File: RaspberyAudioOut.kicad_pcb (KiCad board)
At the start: 2 copper layers, 29 parts, among them J1 Conn_01x04, U1 LM386, U2 LM386

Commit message: Adding PDF of PCB
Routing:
- net GND: track 158.0 -> 26.6 mm

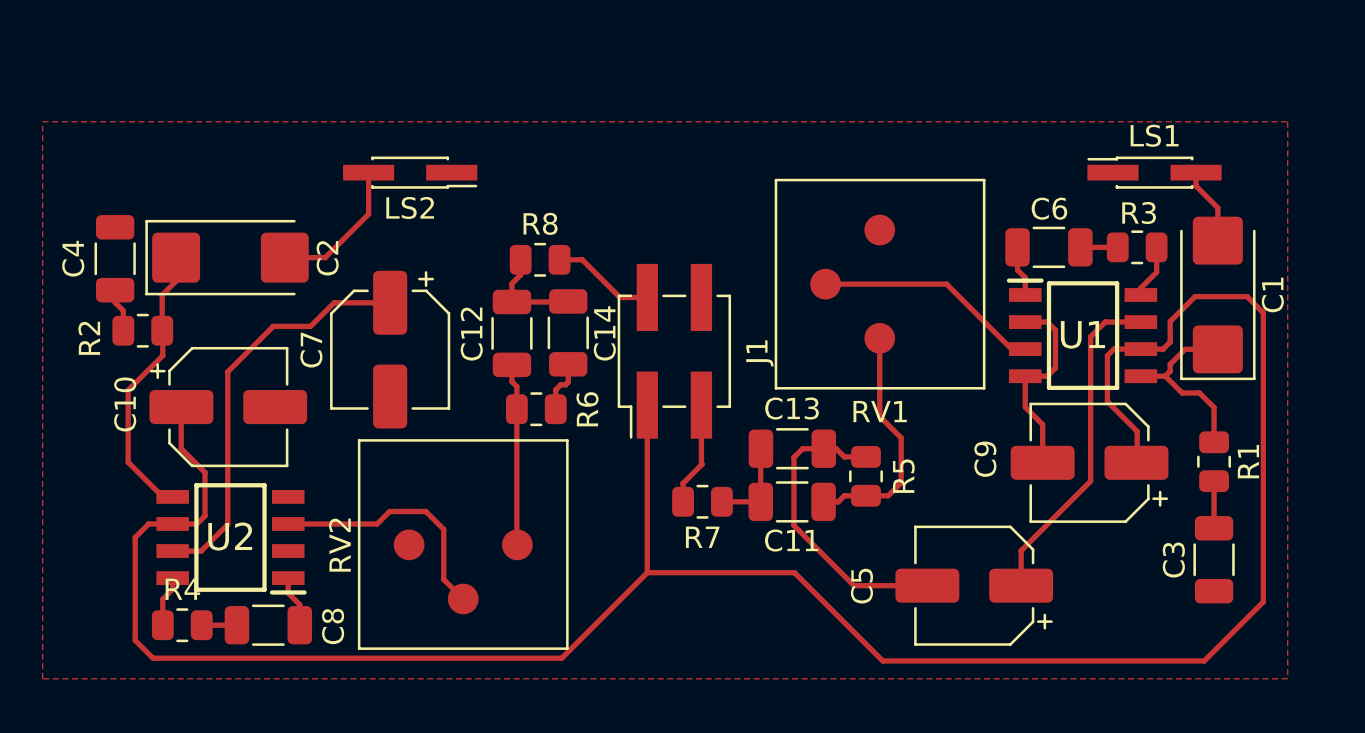
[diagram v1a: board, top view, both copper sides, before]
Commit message: Second step. Changed traces width and some components were added
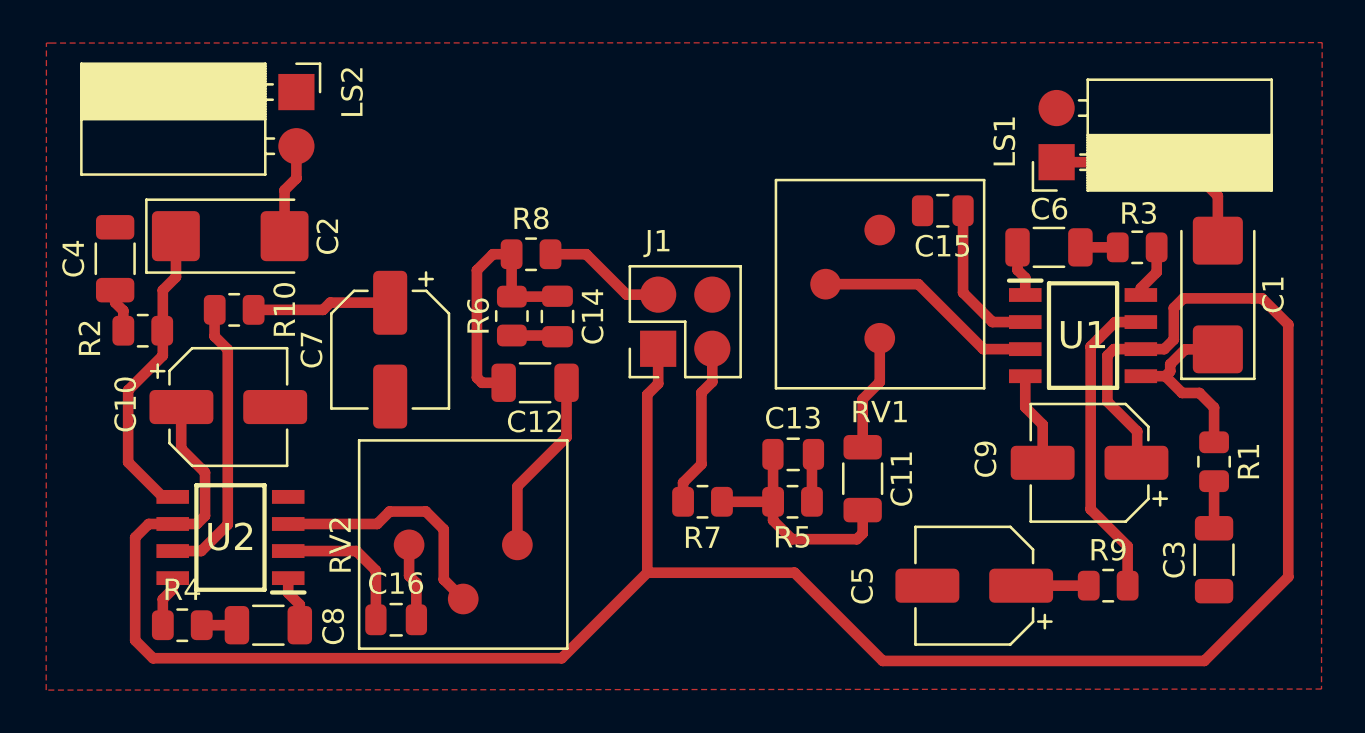
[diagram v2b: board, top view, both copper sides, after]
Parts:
- added C15: 1n, Capacitor_SMD:C_0805_2012Metric, F.Cu at (122.4, 81.2)
- added C16: 1n, Capacitor_SMD:C_0805_2012Metric, F.Cu at (96.8, 100.4)
- added R10: 10k, Resistor_SMD:R_0805_2012Metric, F.Cu at (89.2, 85.9)
- added R9: 10k, Resistor_SMD:R_0805_2012Metric, F.Cu at (130.2, 98.8)
- C13, C14: footprint Capacitor_SMD:C_1206_3216Metric -> Capacitor_SMD:C_0805_2012Metric
- J1: footprint Connector_PinHeader_2.54mm:PinHeader_2x02_P2.54mm_Vertical_SMD -> Connector_PinHeader_2.54mm:PinHeader_2x02_P2.54mm_Vertical
- LS1, LS2: footprint Connector_PinHeader_1.27mm:PinHeader_2x01_P1.27mm_Vertical_SMD -> Connector_PinSocket_2.54mm:PinSocket_1x02_P2.54mm_Horizontal
- moved LS2 6.54 mm to (92.1, 75.7), turned to 0 degrees
- moved LS1 4.62 mm to (127.7, 79.0), turned to 180 degrees
- moved R6 4.52 mm to (102.2, 86.2), turned to -90 degrees
- moved R5 3.65 mm to (115.3, 94.9), turned to 0 degrees
- moved C11 3.48 mm to (118.6, 93.8), turned to -90 degrees
- moved C12 2.56 mm to (103.3, 89.3), turned to 180 degrees
- moved C2 1.01 mm to (89.0, 82.4)
- moved C14 0.92 mm to (104.3, 86.2)
- moved J1 0.77 mm to (109.0, 87.7)
- moved R8 0.50 mm to (103.1, 83.3)
- moved C13 0.27 mm to (115.4, 92.7)
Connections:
- C11 pad 1: Net-(C11-Pad1) -> Net-(RV1-Pad3)
- C12 pad 1: Net-(C12-Pad1) -> Net-(RV2-Pad3)
- C12 pad 2: Net-(C12-Pad2) -> Net-(R6-Pad1)
- C14 pad 1: Net-(C12-Pad2) -> Net-(R6-Pad1)
- LS1 pad 1: GND -> Net-(C1-Pad2)
- LS1 pad 2: Net-(C1-Pad2) -> GND
- R5 pad 1: Net-(C11-Pad1) -> Net-(C11-Pad2)
- R6 pad 1: Net-(C12-Pad1) -> Net-(R6-Pad1)
- R8 pad 1: Net-(C12-Pad2) -> Net-(R6-Pad1)
- RV1 pad 3: Net-(C11-Pad1) -> Net-(RV1-Pad3)
- RV2 pad 3: Net-(C12-Pad1) -> Net-(RV2-Pad3)
- U1 pad 2: GND -> Net-(U1-Pad2)
- U1 pad 7: Net-(C5-Pad1) -> Net-(U1-Pad7)
- U2 pad 2: GND -> Net-(U2-Pad2)
- U2 pad 7: Net-(C7-Pad1) -> Net-(U2-Pad7)
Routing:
- net Net-(U1-Pad7): track 0.00 -> 14.8 mm
- net GND: track 26.6 -> 12.5 mm
- net Net-(U2-Pad7): track 0.00 -> 13.4 mm
- net Net-(C7-Pad1): track 19.2 -> 6.55 mm
- net Net-(C5-Pad1): track 15.7 -> 3.17 mm
- net Net-(R6-Pad1): track 0.00 -> 12.5 mm
- net Net-(C11-Pad1): track 11.2 -> 0.00 mm
- net Net-(RV2-Pad3): track 0.00 -> 8.57 mm
- net Net-(C12-Pad1): track 8.55 -> 0.00 mm
- net Net-(U1-Pad2): track 0.00 -> 7.33 mm
- net Net-(C11-Pad2): track 4.32 -> 11.3 mm
- net Net-(U2-Pad2): track 0.00 -> 6.80 mm
- net Net-(C1-Pad2): track 3.61 -> 10.3 mm
- net Net-(RV1-Pad3): track 0.00 -> 5.44 mm
- net Net-(C12-Pad2): track 4.80 -> 0.00 mm
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
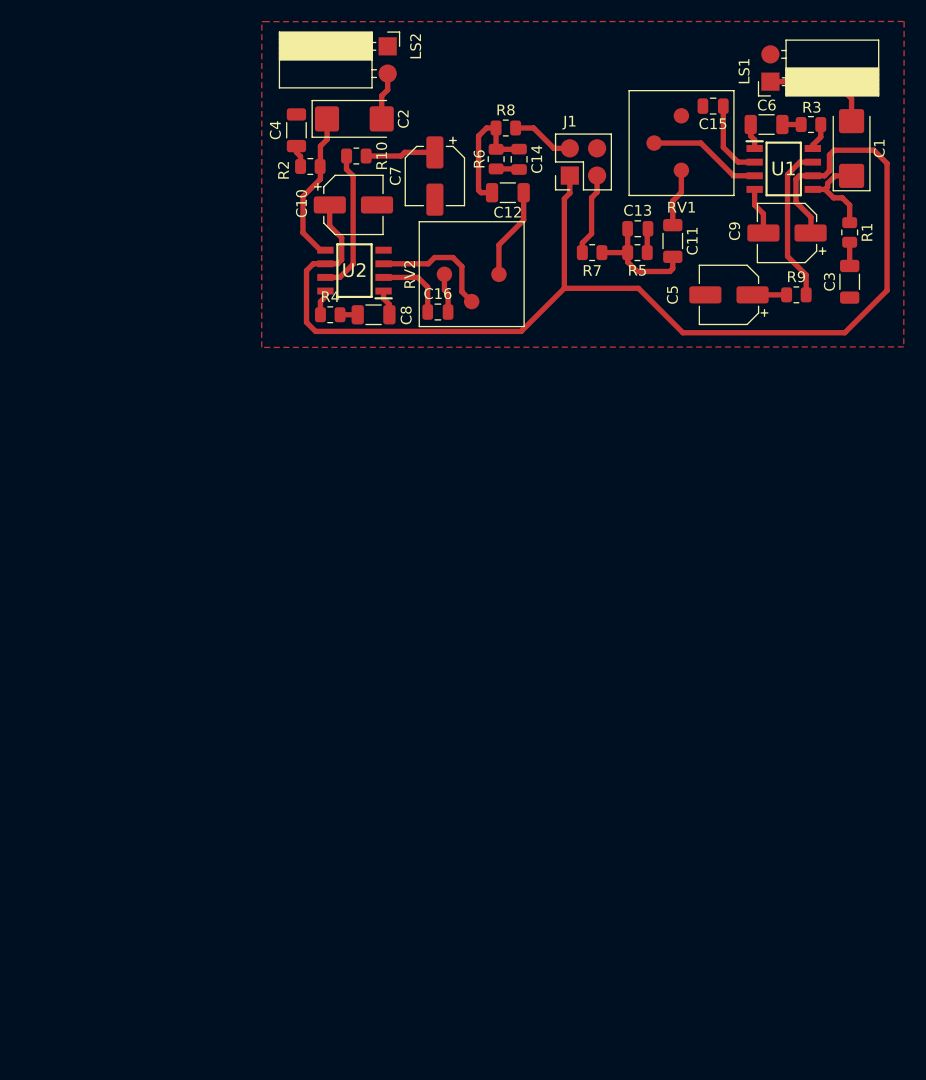
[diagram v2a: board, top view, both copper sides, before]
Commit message: Changed tantal to electrolitic output capacitor
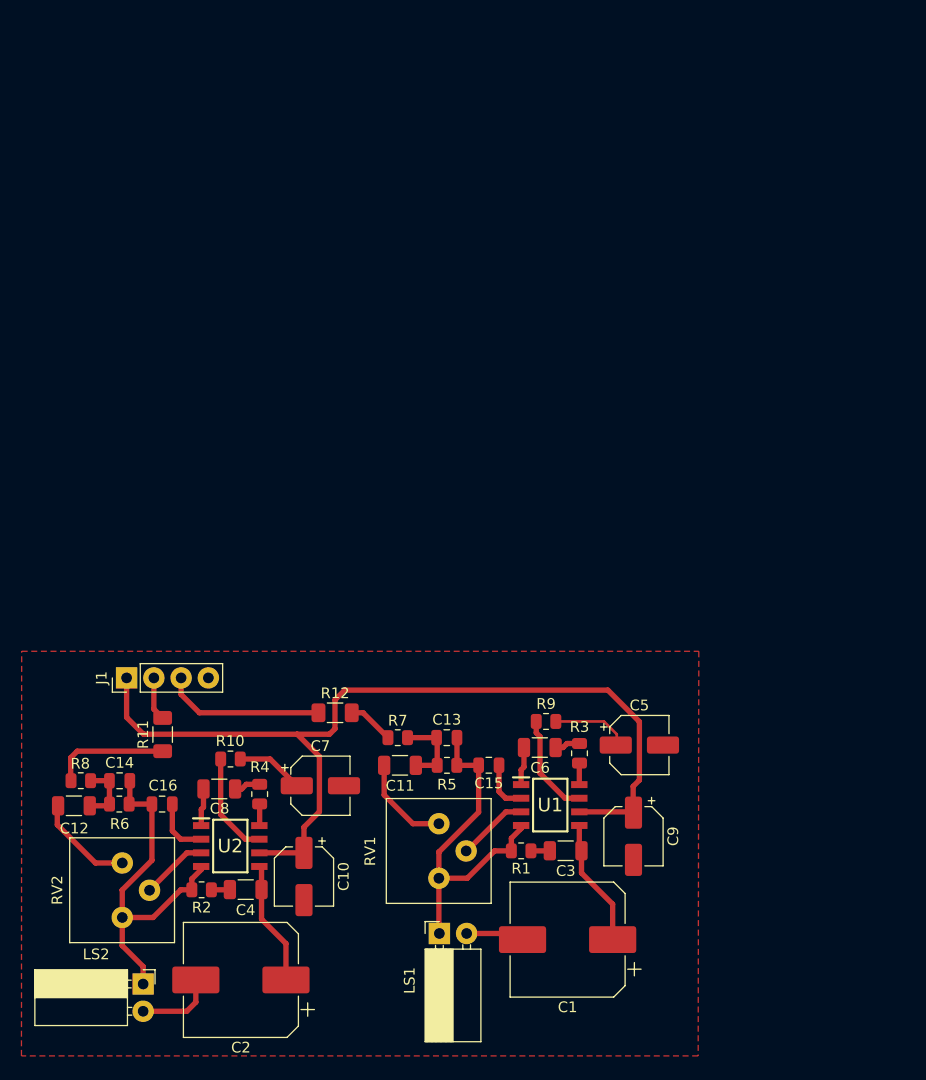
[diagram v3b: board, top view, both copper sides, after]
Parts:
- added R11: 0, Resistor_SMD:R_1206_3216Metric_Pad1.30x1.75mm_HandSolder, F.Cu at (71.1, 139.8)
- added R12: 0, Resistor_SMD:R_1206_3216Metric_Pad1.30x1.75mm_HandSolder, F.Cu at (87.2, 137.8)
- C1, C2: value 220uF -> 1000uF; footprint Capacitor_Tantalum_SMD:CP_EIA-6032-28_Kemet-C_Pad2.25x2.35mm_HandSolder -> Capacitor_SMD:CP_Elec_10x10.5
- J1: footprint Connector_PinHeader_2.54mm:PinHeader_2x02_P2.54mm_Vertical -> Connector_PinHeader_2.54mm:PinHeader_1x04_P2.54mm_Vertical
- U1, U2: footprint LM386:SOIC127P600X175-8N -> LM386MX-1_NOPB:SOIC127P600X175-8N
- moved LS2 90.3 mm to (69.3, 163.1)
- moved LS1 85.2 mm to (96.9, 158.3), turned to 90 degrees
- moved C2 80.9 mm to (78.4, 162.7), turned to 180 degrees
- moved C1 78.3 mm to (108.8, 158.9), turned to 180 degrees
- moved RV1 74.6 mm to (96.8, 153.2), turned to 0 degrees
- moved R8 72.6 mm to (63.5, 144.1), turned to 180 degrees
- moved C4 70.9 mm to (78.8, 154.3), turned to 0 degrees
- moved C12 70.0 mm to (62.8, 146.4), turned to 0 degrees
- moved R6 69.6 mm to (67.1, 146.3), turned to 0 degrees
- moved C14 68.9 mm to (67.1, 144.1), turned to 0 degrees
- moved R2 68.2 mm to (74.7, 154.3)
- moved RV2 67.0 mm to (67.3, 156.9), turned to 0 degrees
- moved R1 65.3 mm to (104.5, 150.7), turned to 180 degrees
- moved C15 64.9 mm to (101.5, 142.7)
- moved U1 63.2 mm to (107.2, 146.4)
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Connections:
- C3 pad 1: GND -> Net-(C3-Pad1)
- C3 pad 2: Net-(C3-Pad2) -> Net-(C1-Pad1)
- C4 pad 1: GND -> Net-(C4-Pad1)
- C4 pad 2: Net-(C4-Pad2) -> Net-(C2-Pad1)
- LS1 pad 1: Net-(C1-Pad2) -> GND
- LS1 pad 2: GND -> Net-(C1-Pad2)
- R1 pad 1: Net-(C1-Pad1) -> Net-(C3-Pad1)
- R1 pad 2: Net-(C3-Pad2) -> GND
- R2 pad 1: Net-(C2-Pad1) -> Net-(C4-Pad1)
- R2 pad 2: Net-(C4-Pad2) -> GND
- R7 pad 2: Net-(J1-Pad3) -> Net-(R7-Pad2)
- R8 pad 2: Net-(J1-Pad2) -> Net-(R8-Pad2)
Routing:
- net GND: track 12.5 -> 65.7 mm
- net +5V: track 112.7 -> 87.2 mm
- net Net-(R8-Pad2): track 0.00 -> 11.0 mm
- net Net-(J1-Pad3): track 7.74 -> 15.0 mm
- net Net-(C12-Pad2): track 12.5 -> 5.84 mm
- net Net-(RV2-Pad2): track 11.5 -> 6.27 mm
- net Net-(R9-Pad2): track 14.8 -> 9.59 mm
- net Net-(C1-Pad2): track 10.3 -> 5.46 mm
- net Net-(R7-Pad2): track 0.00 -> 4.34 mm
- net Net-(C5-Pad1): track 3.17 -> 7.22 mm
- net Net-(RV1-Pad2): track 10.6 -> 6.63 mm
- net Net-(C11-Pad2): track 11.3 -> 7.30 mm
- net Net-(R10-Pad2): track 13.4 -> 9.74 mm
- net Net-(C11-Pad1): track 5.44 -> 8.97 mm
- net Net-(C1-Pad1): track 8.85 -> 11.9 mm
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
